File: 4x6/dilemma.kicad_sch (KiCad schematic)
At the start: 250 parts, among them J1 USB_C_Receptacle_USB2.0, J102 NA_serial, J105 NA_Conn_01x04_Female, J113 Cirque, J2 NA_Conn_01x03_Female, J3 NA_GC9A01, J4 Conn_01x05, J5 NA_Conn_01x02, J5001 USB_C_Receptacle_USB2.0, J5002 NA_Conn_01x02, J5003 NA_serial, J5004 NA_GC9A01, J5005 NA_Conn_01x04_Female, J5006 NA_Conn_01x03_Female, J5007 Cirque, J5008 Conn_01x05, J5009 Conn_01x05, J5010 Conn_01x05, SW1 SW_Push, SW101 NA_SW_Push, SW102 NA_SW_Push, SW103 NA_SW_Push, SW104 NA_SW_Push, SW105 NA_SW_Push, SW106 NA_SW_Push, SW107 NA_SW_Push, SW108 NA_SW_Push, SW109 NA_SW_Push, SW112 NA_SW_Push, SW113 NA_SW_Push, SW114 NA_SW_Push, SW115 NA_SW_Push, SW116 NA_SW_Push, SW117 NA_SW_Push, SW118 NA_SW_Push, SW119 NA_SW_Push, SW3001 NA_SW_Push, SW3002 NA_RotaryEncoder_Switch, SW5001 SW_Push, SW5002 NA_SW_Push, SW5003 NA_SW_Push, SW5004 NA_SW_Push, SW5005 NA_SW_Push, SW5006 NA_SW_Push, SW5007 NA_SW_Push, SW5008 NA_SW_Push, SW5009 NA_SW_Push, SW5010 NA_SW_Push, SW5011 NA_SW_Push, SW5012 NA_SW_Push, SW5013 NA_SW_Push, SW5014 NA_SW_Push, SW5015 NA_SW_Push, SW5016 NA_SW_Push, SW5017 NA_SW_Push, SW5018 NA_SW_Push, SW5019 NA_SW_Push, SW5020 NA_RotaryEncoder_Switch, SW5021 SW_SPST, SW5022 SW_SPST, U1 RP2040, U2 W25Q128JVS, U3 XC6210B332MR-G, U4 USBLC6-2P6, U5001 XC6210B332MR-G, U5002 RP2040, U5003 USBLC6-2P6, U5004 W25Q128JVS, Y1 Crystal_GND24, Y5001 Crystal_GND24

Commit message: change diodes
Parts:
- removed D30, D31, D32, D33, D34, D35, D36, D37, D5002, D5003, D5005, D5006, D5007, D5008, D5010, D5012: D_CC, local-libraries:SOT-323_SC-70, symbol Device:D_Dual_CommonCathode_AAK
- added D5002, D5003, D5005, D5006, D5007, D5008, D5010, D5012, D5067, D5068, D5069, D5070, D5071, D5072, D5073, D5074, D5075, D5076, D5077, D5078, D5079, D5080, D5081, D5082, D5083, D5084, D5085, D5086, D5087, D5088, D5089, D5090: D, local-libraries:D_SOD-323, symbol Device:D
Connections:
- net M_COL1: now also D5067.1 (K), D5068.1 (K), D5069.1 (K), D5070.1 (K)
- net M_COL1_L: now also D5002.1 (K), D5003.1 (K), D5083.1 (K), D5084.1 (K)
- net M_COL2: now also D5071.1 (K), D5072.1 (K), D5073.1 (K), D5074.1 (K)
- net M_COL2_L: now also D5005.1 (K), D5006.1 (K), D5085.1 (K), D5086.1 (K)
- net M_COL3: now also D5075.1 (K), D5076.1 (K), D5081.1 (K), D5082.1 (K)
- net M_COL3_L: now also D5007.1 (K), D5008.1 (K), D5087.1 (K), D5088.1 (K)
- net M_COL4: now also D5077.1 (K), D5078.1 (K)
- net M_COL4_L: now also D5010.1 (K), D5089.1 (K)
- net M_COL5: now also D5079.1 (K), D5080.1 (K)
- net M_COL5_L: now also D5012.1 (K), D5090.1 (K)
- net encoder_diode: now also D5082.2 (A)
- net encoder_diode_L: now also D5088.2 (A)
- net at SW5003.2: now also D5083.2 (A)
- net at SW118.2: now also D5070.2 (A)
- net at SW109.2: now also D5081.2 (A)
- net at SW105.2: now also D5072.2 (A)
- net at SW108.2: now also D5076.2 (A)
- net at SW107.2: now also D5075.2 (A)
- net at SW5011.2: now also D5087.2 (A)
- net at SW5010.2: now also D5007.2 (A)
- net at SW5012.2: now also D5008.2 (A)
- net at SW102.2: now also D5068.2 (A)
- net at SW5005.2: now also D5084.2 (A)
- net at SW5004.2: now also D5003.2 (A)
- net at SW115.2: now also D5079.2 (A)
- net at SW116.2: now also D5080.2 (A)
- net at SW104.2: now also D5071.2 (A)
- net at SW119.2: now also D5074.2 (A)
- net at SW106.2: now also D5073.2 (A)
- net at SW5009.2: now also D5085.2 (A)
- net at SW5018.2: now also D5090.2 (A)
- net at SW5017.2: now also D5012.2 (A)
- net at SW113.2: now also D5078.2 (A)
- net at SW112.2: now also D5077.2 (A)
- net at SW5002.2: now also D5002.2 (A)
- net at SW5014.2: now also D5010.2 (A)
- net at SW101.2: now also D5067.2 (A)
- net at SW5007.2: now also D5086.2 (A)
- net at SW5006.2: now also D5005.2 (A)
- net at SW5015.2: now also D5089.2 (A)
- net at SW5008.2: now also D5006.2 (A)
- net at SW103.2: now also D5069.2 (A)
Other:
- moved on the sheet: SW5002, SW5003, SW5004, SW5005, SW5006, SW5007, SW5008, SW5009, SW5010, SW5011, SW5012, SW5013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

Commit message: schem switches
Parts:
- added D5091, D5092, D5093, D5094, D5095, D5096, D5097, D5098, D5099, D5100, D5101, D5102, D5103, D5104, D5105, D5106, D5107, D5108: D, local-libraries:D_SOD-323, symbol Device:D
- added SW5023, SW5024, SW5025, SW5026, SW5027, SW5028, SW5029, SW5030, SW5031, SW5032, SW5033, SW5034, SW5035, SW5036, SW5037, SW5038, SW5039, SW5040: NA_SW_Push, local-libraries:SW_MX_choc, symbol Switch:SW_Push
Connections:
- net M_COL1: now also D5091.1 (K)
- net M_COL1_L: now also D5103.1 (K)
- net M_COL2: now also D5092.1 (K)
- net M_COL2_L: now also D5104.1 (K)
- net M_COL3: now also D5093.1 (K)
- net M_COL3_L: now also D5105.1 (K)
- net M_COL4: now also D5094.1 (K)
- net M_COL4_L: now also D5106.1 (K)
- net M_COL5: now also D5095.1 (K)
- net M_COL5_L: now also D5107.1 (K)
- net M_ROW2: now also SW5029.1
- net M_ROW2_L: now also SW5032.1
- net M_ROW3: now also SW5030.1
- net M_ROW3_L: now also SW5033.1
- net M_ROW4: now also SW5031.1
- net M_ROW4_L: now also SW5034.1
- new net: D5094.2 (A), SW5026.2
- new net: D5100.2 (A), SW5034.2
- new net: D5105.2 (A), SW5037.2
- new net: D5102.2 (A), SW5033.2
- new net: D5095.2 (A), SW5027.2
- new net: D5097.2 (A), SW5028.2
- new net: D5096.2 (A), SW5031.2
- new net: D5098.2 (A), SW5029.2
- new net: D5106.2 (A), SW5038.2
- new net: D5101.2 (A), SW5032.2
- new net: D5104.2 (A), SW5036.2
- new net: D5103.2 (A), SW5035.2
- new net: D5107.2 (A), SW5039.2
- new net: D5093.2 (A), SW5025.2
- new net: D5092.2 (A), SW5024.2
- new net: D5091.2 (A), SW5023.2
- new net: D5108.2 (A), SW5040.2
- new net: D5099.2 (A), SW5030.2
- new net M_COL6: D5096.1 (K), D5097.1 (K), D5098.1 (K), D5099.1 (K)
- new net M_COL6_L: D5100.1 (K), D5101.1 (K), D5102.1 (K), D5108.1 (K)
- new net M_ROW5: SW5023.1, SW5024.1, SW5025.1, SW5026.1, SW5027.1, SW5028.1
- new net M_ROW5_L: SW5035.1, SW5036.1, SW5037.1, SW5038.1, SW5039.1, SW5040.1
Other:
- moved on the sheet: D5002, D5003, D5005, D5007, D5008, D5010, D5012, D5067, D5068, D5069, D5070, D5071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

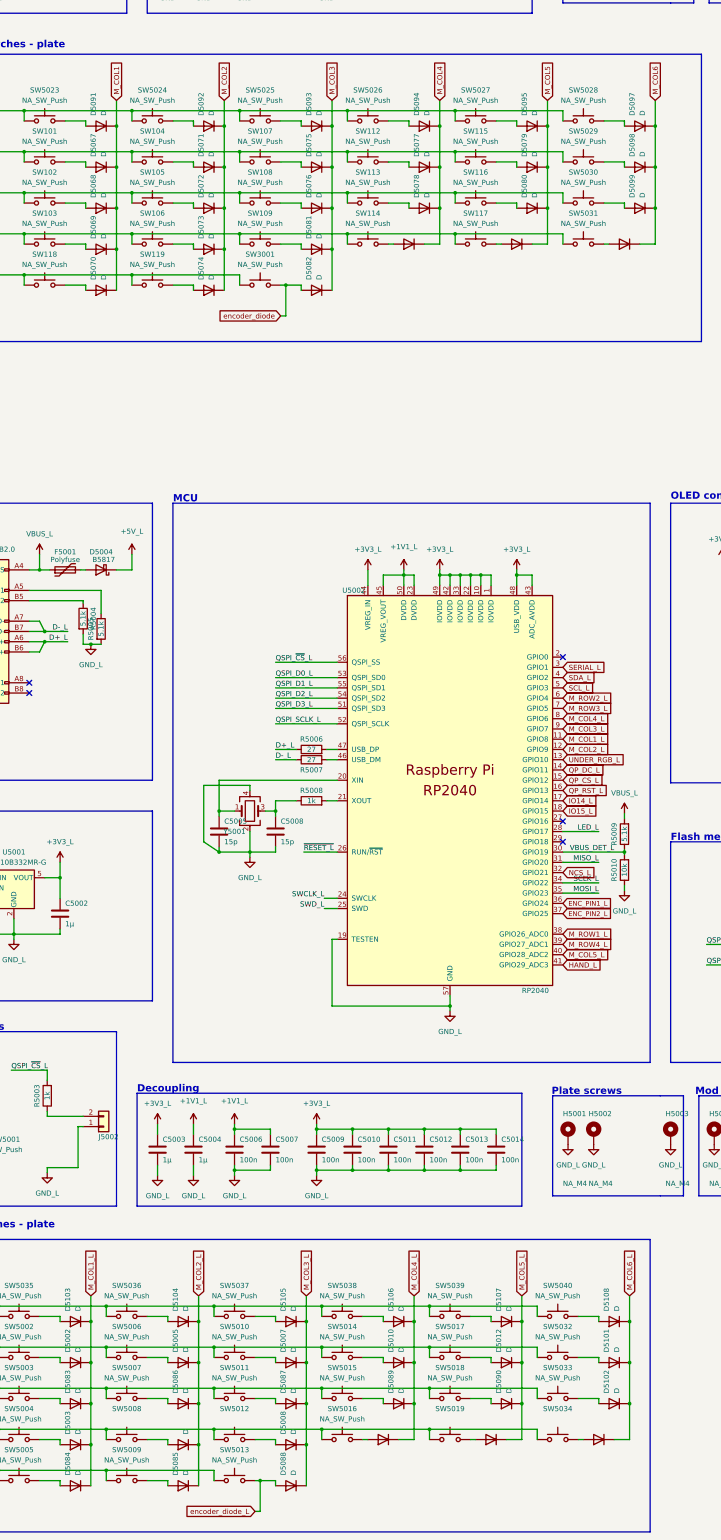
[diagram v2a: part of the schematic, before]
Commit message: add diodes
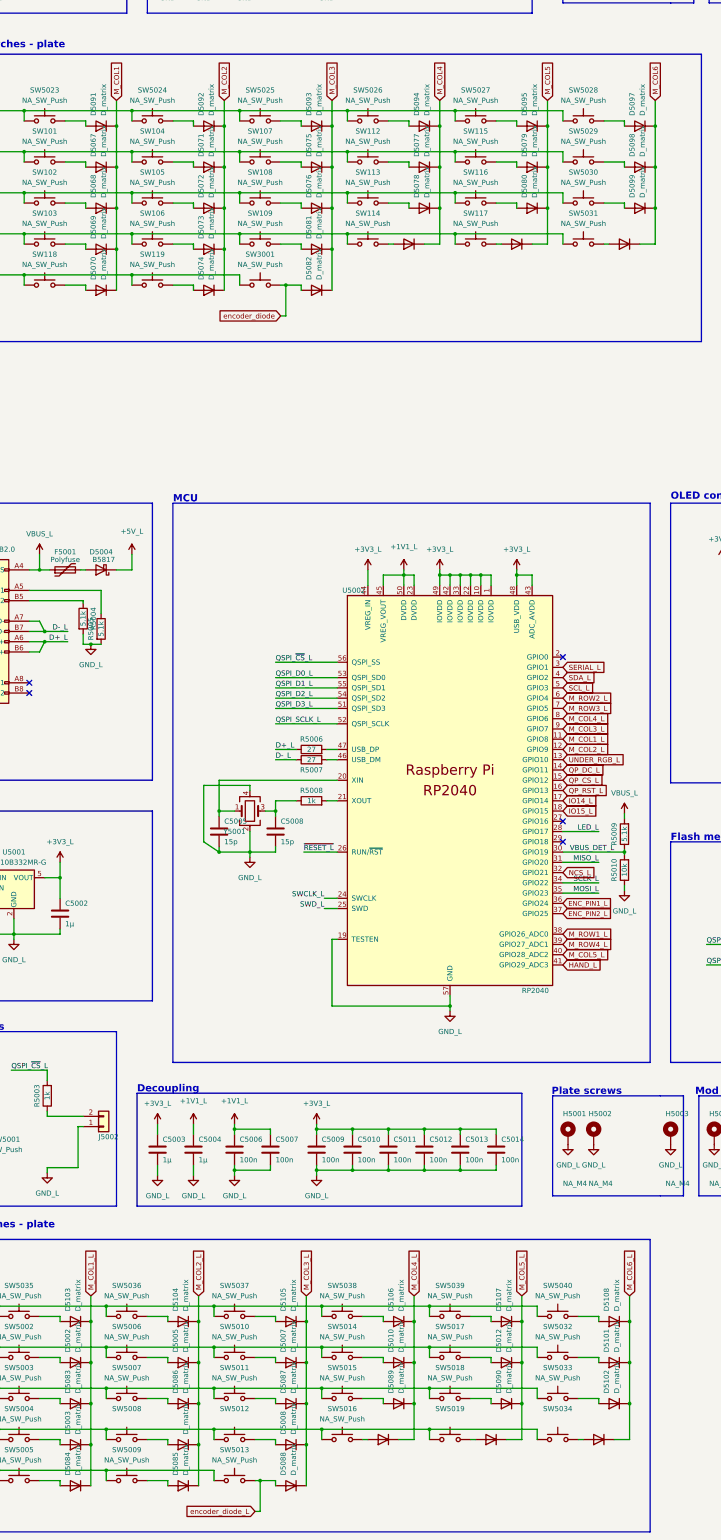
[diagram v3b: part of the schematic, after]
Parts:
- D112, D115, D5002, D5003, D5005, D5006, D5007, D5008, D5009, D5010, D5011, D5012, D5067, D5068, D5069, D5070, D5071, D5072, D5073, D5074, D5075, D5076, D5077, D5078, D5079, D5080, D5081, D5082, D5083, D5084, D5085, D5086, D5087, D5088, D5089, D5090, D5091, D5092, D5093, D5094, D5095, D5096, D5097, D5098, D5099, D5100, D5101, D5102, D5103, D5104, D5105, D5106, D5107, D5108: value D -> D_matrix; footprint local-libraries:D_SOD-323 -> local-libraries:D_0402

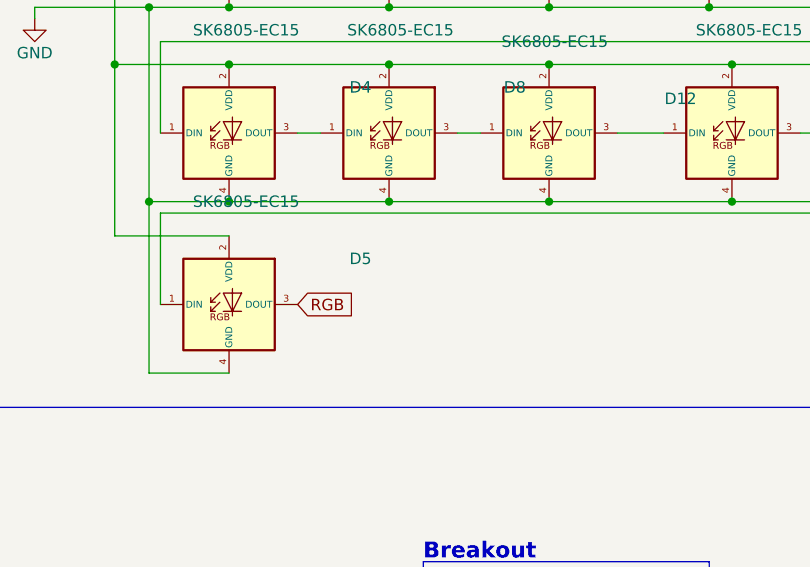
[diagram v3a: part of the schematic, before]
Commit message: place and fill in ec15 leds
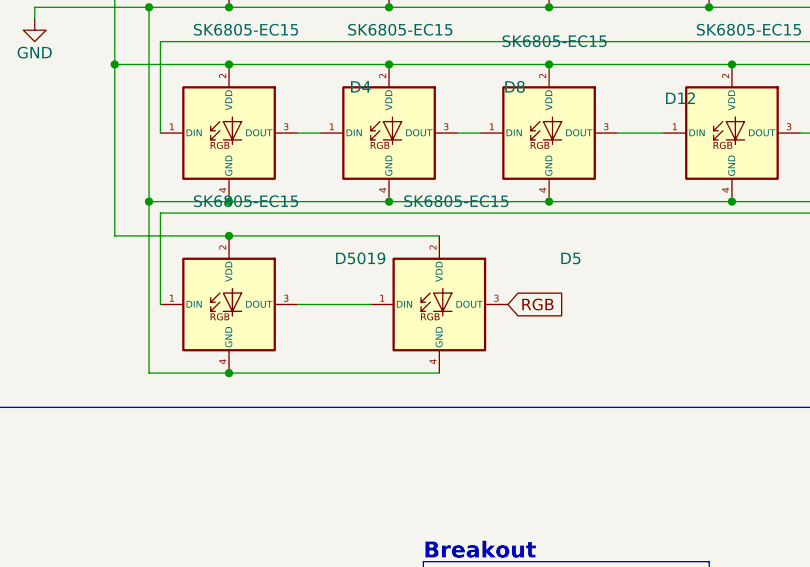
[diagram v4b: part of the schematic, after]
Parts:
- added D5: SK6805-EC15, 0xB2_drawings:LED_SK6805-EC15_1.5x1.5mm_P0.6mm_handsolder(1), symbol sk6805-ec15:SK6805-EC15
- renumbered D5 to D5019
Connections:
- net +3V3: now also D5.2 (VDD)
- net GND: now also D5.4 (GND)
- net RGB: now also D5.3 (DOUT); no longer D5019.3 (DOUT)
- new net: D5.1 (DIN), D5019.3 (DOUT)
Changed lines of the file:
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@@
   (junction (at 455.93 41.91) (diameter 0) (color 0 0 0 0)
   )
+  (junction (at 402.59 67.31) (diameter 0) (color 0 0 0 0)
+  )
   (junction (at 148.59 185.42) (diameter 0) (color 0 0 0 0)
   )
@@
   (junction (at 402.59 48.26) (diameter 0) (color 0 0 0 0)
   )
+  (junction (at 402.59 82.55) (diameter 0) (color 0 0 0 0)
+  )
   (junction (at 130.81 185.42) (diameter 0) (color 0 0 0 0)
   )
@@
     (stroke (width 0) (type default))
   )
+  (wire (pts (xy 402.59 67.31) (xy 425.958 67.31))
+    (stroke (width 0) (type default))
+  )
   (wire (pts (xy 116.84 518.16) (xy 116.84 528.32))
     (stroke (width 0) (type default))
@@
     (stroke (width 0) (type default))
   )
+  (wire (pts (xy 402.59 82.55) (xy 425.958 82.55))
+    (stroke (width 0) (type default))
+  )
   (wire (pts (xy 111.76 96.52) (xy 111.76 97.79))
     (stroke (width 0) (type default))
@@
     (stroke (width 0) (type default))
   )
+  (wire (pts (xy 410.21 74.93) (xy 418.338 74.93))
+    (stroke (width 0) (type default))
+  )
   (wire (pts (xy 127 220.98) (xy 127 218.44))
     (stroke (width 0) (type default))
@@
     )
   )
-  (global_label "RGB" (shape input) (at 410.21 74.93 0)
+  (global_label "RGB" (shape input) (at 433.578 74.93 0)
     (effects (font (size 1.27 1.27)) (justify left))
-    (property "Intersheetrefs" "${INTERSHEET_REFS}" (at 497.84 142.24 0)
+    (property "Intersheetrefs" "${INTERSHEET_REFS}" (at 521.208 142.24 0)
       (effects (font (size 1.27 1.27)) hide)
     )
@@
     )
   )
+  (symbol (lib_id "sk6805-ec15:SK6805-EC15") (at 425.958 74.93 0) (unit 1)
+    (in_bom yes) (on_board yes) (dnp no)
+    (property "Reference" "D5" (at 440.563 69.85 0)
+      (effects (font (size 1.27 1.27)))
+    )
+    (property "Value" "SK6805-EC15" (at 427.863 63.5 0)
+      (effects (font (size 1.27 1.27)))
+    )
+    (property "Footprint" "0xB2_drawings:LED_SK6805-EC15_1.5x1.5mm_P0.6mm_handsolder(1)" (at 427.228 82.55 0)
+      (effects (font (size 1.27 1.27)) (justify left top) hide)
+    )
+    (property "Datasheet" "https://datasheet.lcsc.com/lcsc/2108251530_OPSCO-Optoelectronics-SK6805-EC15_C2890035.pdf" (at 428.498 84.455 0)
+      (effects (font (size 1.27 1.27)) (justify left top) hide)
+    )
+    (property "MFN" "Dongguan Opsco Optoelectronics" (at 425.958 59.055 0)
+      (effects (font (size 1.27 1.27)) hide)
+    )
+    (property "MPN" "SK6805-EC15" (at 425.958 61.8301 0)
+      (effects (font (size 1.27 1.27)) hide)
+    )
+    (property "PKG" "SK6805-EC15" (at 425.958 64.6052 0)
+      (effects (font (size 1.27 1.27)) hide)
+    )
+    (property "LCSC" "C2890035" (at 425.958 74.93 0)
+      (effects (font (size 1.27 1.27)) hide)
+    )
+    (pin "1")
+    (pin "2")
+    (pin "3")
+    (pin "4")
+    (instances
+      (project "dilemma"
+        (path "/7353e96a-343a-4876-b497-b1d205a14d97"
+          (reference "D5") (unit 1)
+        )
+      )
+    )
+  )
   (symbol (lib_id "Device:D") (at 86.36 528.32 180) (unit 1)
     (in_bom yes) (on_board yes) (dnp no)
@@
   (symbol (lib_id "sk6805-ec15:SK6805-EC15") (at 402.59 74.93 0) (unit 1)
     (in_bom yes) (on_board yes) (dnp no)
-    (property "Reference" "D5" (at 417.195 69.85 0)
+    (property "Reference" "D5019" (at 417.195 69.85 0)
       (effects (font (size 1.27 1.27)))
     )
@@
       (project "dilemma"
         (path "/7353e96a-343a-4876-b497-b1d205a14d97"
-          (reference "D5") (unit 1)
+          (reference "D5019") (unit 1)
         )
       )

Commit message: cleanup traces
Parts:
- added D5015, D5110, D5111, D5112, D5114, D5115, D5116: SK6805-EC15, local-libraries:LED_SK6805-EC15_1.5x1.5mm_P0.6mm_handsolder, symbol sk6805-ec15:SK6805-EC15
- D11, D12, D15, D16, D18, D19, D21, D22, D24, D25, D27, D28, D3, D4, D5, D5013, D5014, D5016, D5017, D5018, D5019, D5020, D5021, D5022, D5023, D5024, D5025, D5026, D5027, D5028, D5029, D5030, D7, D8, D9: footprint 0xB2_drawings:LED_SK6805-EC15_1.5x1.5mm_P0.6mm_handsolder(1) -> local-libraries:LED_SK6805-EC15_1.5x1.5mm_P0.6mm_handsolder
- D5109: renamed from D5019; footprint 0xB2_drawings:LED_SK6805-EC15_1.5x1.5mm_P0.6mm_handsolder(1) -> local-libraries:LED_SK6805-EC15_1.5x1.5mm_P0.6mm_handsolder
- D5113: renamed from D5015; footprint 0xB2_drawings:LED_SK6805-EC15_1.5x1.5mm_P0.6mm_handsolder(1) -> local-libraries:LED_SK6805-EC15_1.5x1.5mm_P0.6mm_handsolder
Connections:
- net +3V3: now also D5110.2 (VDD), D5111.2 (VDD), D5112.2 (VDD)
- net +3V3_L: now also D5015.2 (VDD), D5114.2 (VDD), D5115.2 (VDD), D5116.2 (VDD)
- net GND: now also D5110.4 (GND), D5111.4 (GND), D5112.4 (GND)
- net GND_L: now also D5015.4 (GND), D5114.4 (GND), D5115.4 (GND), D5116.4 (GND)
- net RGB_L: now also D5015.3 (DOUT); no longer D5113.3 (DOUT)
- net at D27.1 (DIN): now also D5112.3 (DOUT); no longer D24.3 (DOUT)
- net at D27.3 (DOUT): no longer D4.1 (DIN)
- net at D5024.1 (DIN): now also D5116.3 (DOUT); no longer D5022.3 (DOUT)
- net at D5020.3 (DOUT): now also D5114.1 (DIN); no longer D5022.1 (DIN)
- net at D15.3 (DOUT): now also D5110.1 (DIN); no longer D18.1 (DIN)
- net at D18.3 (DOUT): now also D5111.1 (DIN); no longer D21.1 (DIN)
- new net: D24.3 (DOUT), D5112.1 (DIN)
- new net: D5015.1 (DIN), D5113.3 (DOUT)
- new net: D5115.3 (DOUT), D5116.1 (DIN)
- new net: D21.1 (DIN), D5111.3 (DOUT)
- new net: D5022.1 (DIN), D5114.3 (DOUT)
- new net: D18.1 (DIN), D5110.3 (DOUT)
- new net: D5022.3 (DOUT), D5115.1 (DIN)
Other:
- moved on the sheet: C5017, C5018, D18, D21, D24, D27, D5022, D5024, D5026, D5028, D5031, D5032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
